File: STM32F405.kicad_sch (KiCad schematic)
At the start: 27 parts, among them SW1 SW_MEC_5G, SW2 SW_DIP_x04, U6 STM32F405RGTx, Y1 25MHz

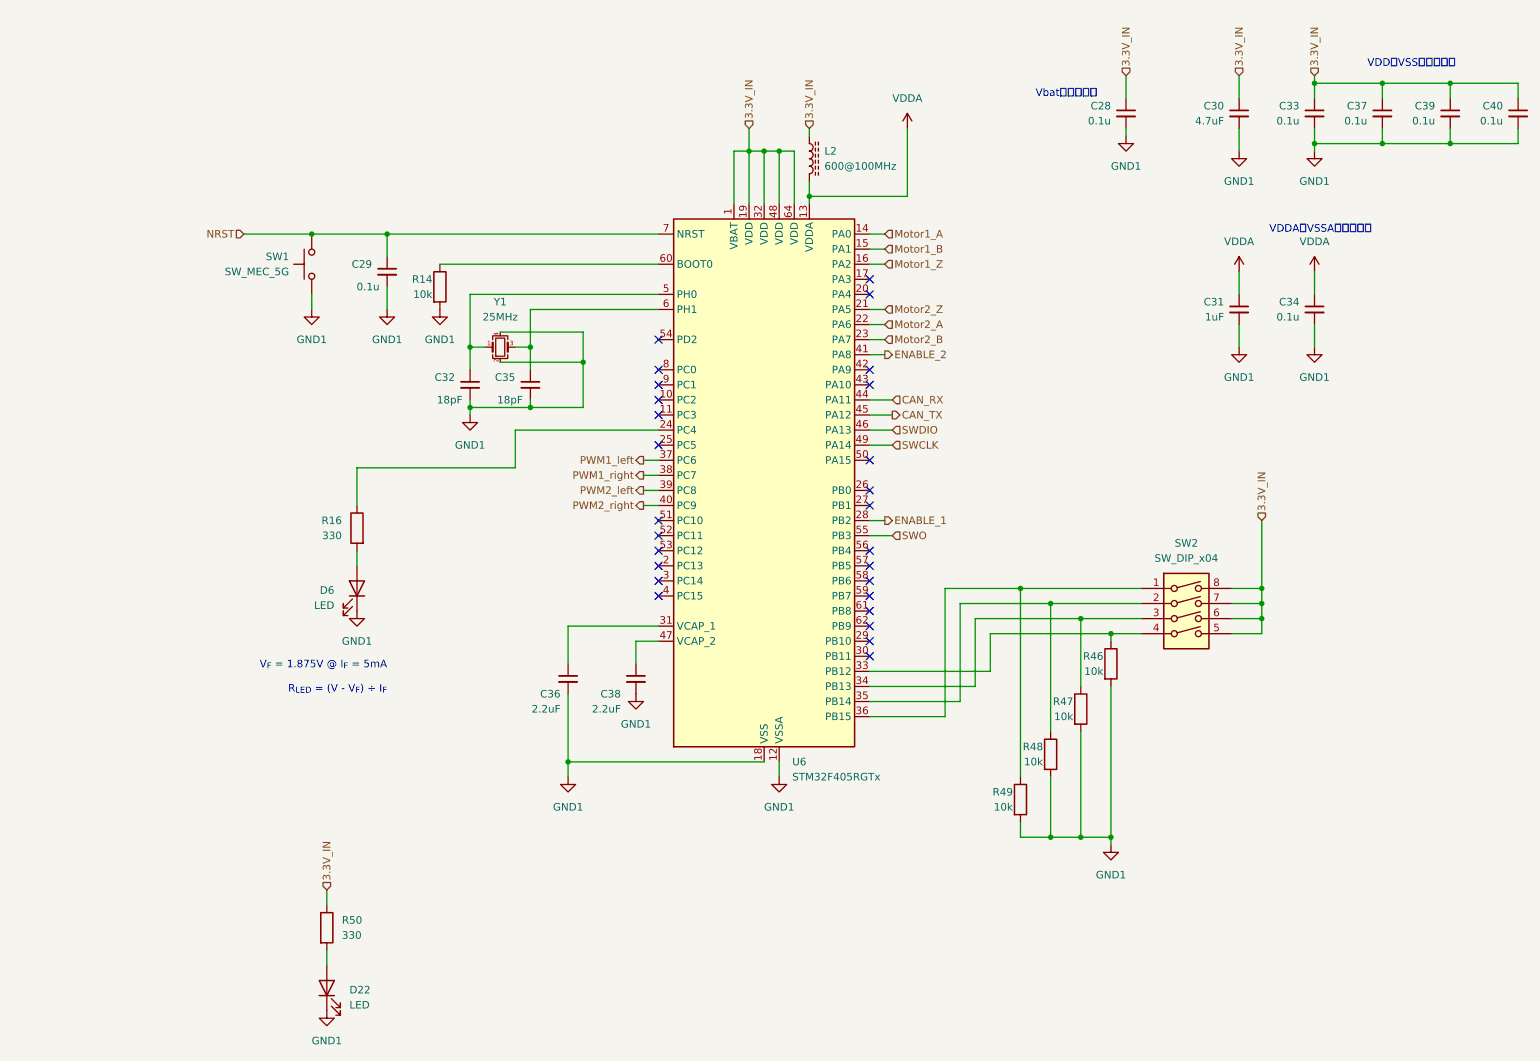
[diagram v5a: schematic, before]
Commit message: Update PCB design & add microSD connector
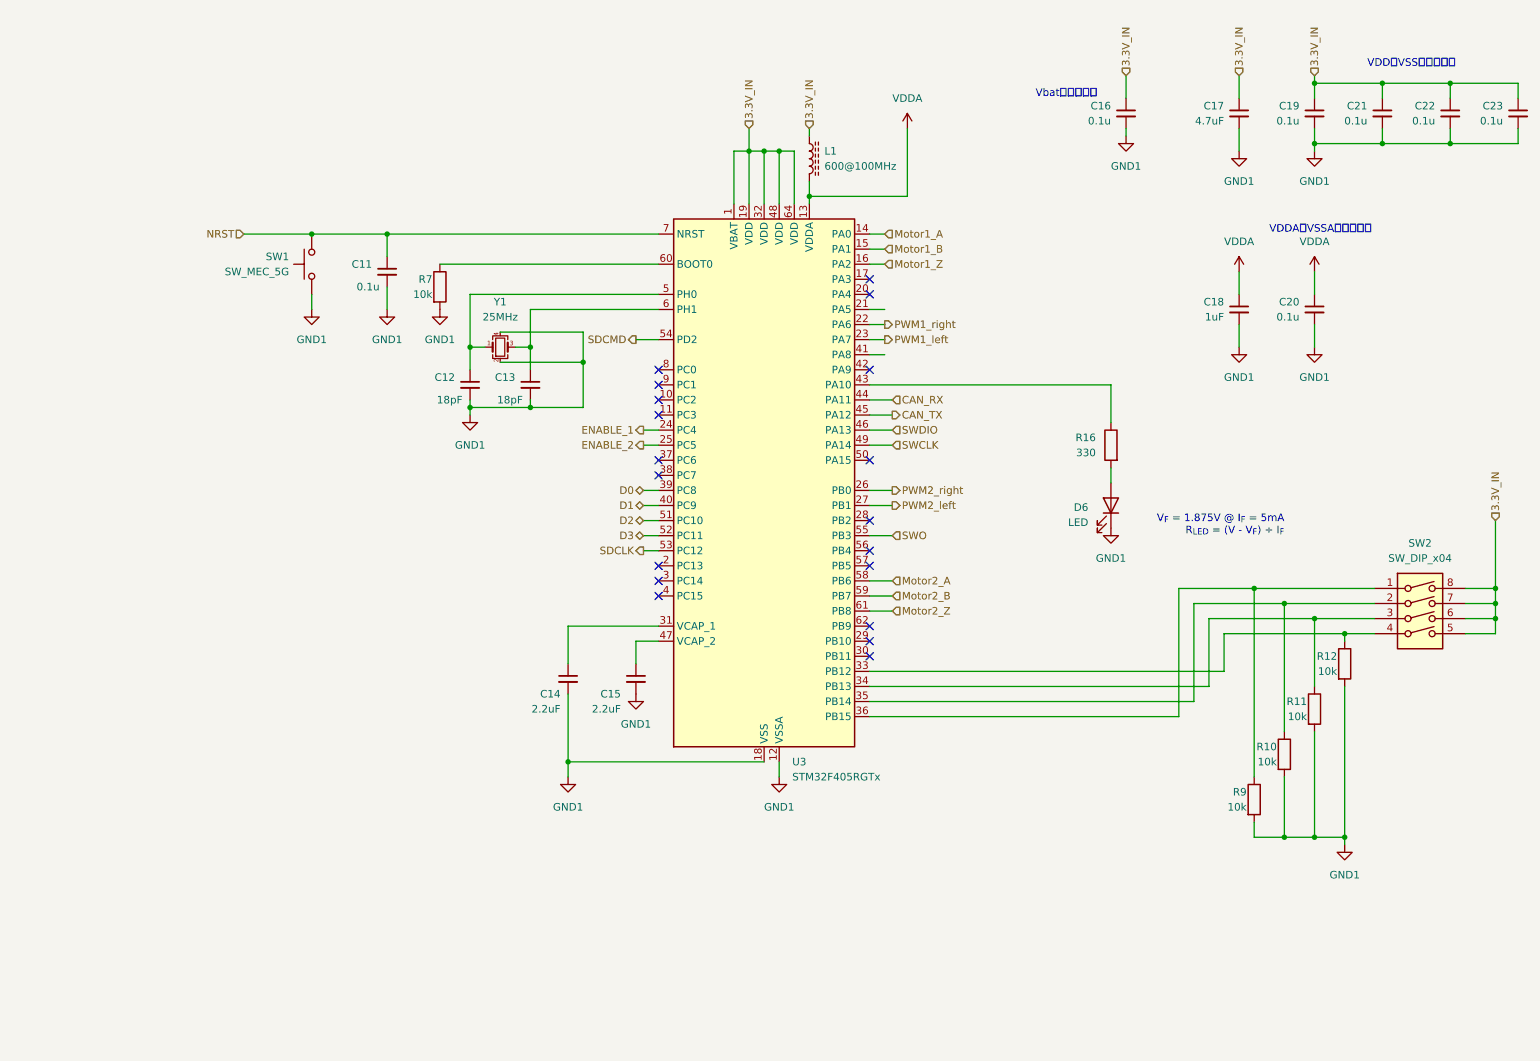
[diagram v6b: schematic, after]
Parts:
- removed D22: LED, LED_SMD:LED_0603_1608Metric_Pad1.05x0.95mm_HandSolder, symbol Device:LED
- removed R50: 330, Resistor_SMD:R_0603_1608Metric_Pad0.98x0.95mm_HandSolder, symbol Device:R
- C11: renamed from C29; footprint Capacitor_SMD:C_0402_1005Metric_Pad0.74x0.62mm_HandSolder -> Capacitor_SMD:C_0402_1005Metric
- C14: renamed from C36; footprint Capacitor_SMD:C_0603_1608Metric_Pad1.08x0.95mm_HandSolder -> Capacitor_SMD:C_0603_1608Metric
- C15: renamed from C38; footprint Capacitor_SMD:C_0603_1608Metric_Pad1.08x0.95mm_HandSolder -> Capacitor_SMD:C_0603_1608Metric
- C16: renamed from C28; footprint Capacitor_SMD:C_0402_1005Metric_Pad0.74x0.62mm_HandSolder -> Capacitor_SMD:C_0402_1005Metric
- C17: renamed from C30; footprint Capacitor_SMD:C_0603_1608Metric_Pad1.08x0.95mm_HandSolder -> Capacitor_SMD:C_0402_1005Metric
- C18: renamed from C31; footprint Capacitor_SMD:C_0603_1608Metric_Pad1.08x0.95mm_HandSolder -> Capacitor_SMD:C_0402_1005Metric
- C19: renamed from C33; footprint Capacitor_SMD:C_0402_1005Metric_Pad0.74x0.62mm_HandSolder -> Capacitor_SMD:C_0402_1005Metric
- C20: renamed from C34; footprint Capacitor_SMD:C_0402_1005Metric_Pad0.74x0.62mm_HandSolder -> Capacitor_SMD:C_0402_1005Metric
- C21: renamed from C37; footprint Capacitor_SMD:C_0402_1005Metric_Pad0.74x0.62mm_HandSolder -> Capacitor_SMD:C_0402_1005Metric
- C22: renamed from C39; footprint Capacitor_SMD:C_0402_1005Metric_Pad0.74x0.62mm_HandSolder -> Capacitor_SMD:C_0402_1005Metric
- C23: renamed from C40; footprint Capacitor_SMD:C_0402_1005Metric_Pad0.74x0.62mm_HandSolder -> Capacitor_SMD:C_0402_1005Metric
- L1: renamed from L2; footprint Resistor_SMD:R_0805_2012Metric_Pad1.20x1.40mm_HandSolder -> Resistor_SMD:R_0805_2012Metric
- R10: renamed from R48; footprint Resistor_SMD:R_0402_1005Metric_Pad0.72x0.64mm_HandSolder -> Resistor_SMD:R_0402_1005Metric
- R11: renamed from R47; footprint Resistor_SMD:R_0402_1005Metric_Pad0.72x0.64mm_HandSolder -> Resistor_SMD:R_0402_1005Metric
- R12: renamed from R46; footprint Resistor_SMD:R_0402_1005Metric_Pad0.72x0.64mm_HandSolder -> Resistor_SMD:R_0402_1005Metric
- R16: footprint Resistor_SMD:R_0603_1608Metric_Pad0.98x0.95mm_HandSolder -> Resistor_SMD:R_0603_1608Metric
- R7: renamed from R14; footprint Resistor_SMD:R_0402_1005Metric_Pad0.72x0.64mm_HandSolder -> Resistor_SMD:R_0402_1005Metric
- R9: renamed from R49; footprint Resistor_SMD:R_0402_1005Metric_Pad0.72x0.64mm_HandSolder -> Resistor_SMD:R_0402_1005Metric
- SW1: footprint Button_Switch_SMD:SW_Push_1P1T_XKB_TS-1187A -> RDC_footprint:TVBP06-B043
- renumbered C32 to C12, C35 to C13, U6 to U3
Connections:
- net ENABLE_1: now also U3.24 (PC4); no longer U3.28 (PB2)
- net ENABLE_2: now also U3.25 (PC5); no longer U3.41 (PA8)
- net Motor2_A: now also U3.58 (PB6); no longer U3.22 (PA6)
- net Motor2_B: now also U3.59 (PB7); no longer U3.23 (PA7)
- net Motor2_Z: now also U3.61 (PB8); no longer U3.21 (PA5)
- net PWM1_left: now also U3.23 (PA7); no longer U3.37 (PC6)
- net PWM1_right: now also U3.22 (PA6); no longer U3.38 (PC7)
- net PWM2_left: now also U3.27 (PB1); no longer U3.39 (PC8)
- net PWM2_right: now also U3.26 (PB0); no longer U3.40 (PC9)
- net at R16.1: now also U3.43 (PA10); no longer U3.24 (PC4)
- net D2: now reaches U3.51 (PC10)
- net D3: now reaches U3.52 (PC11)
- net SDCLK: now reaches U3.53 (PC12)
- net SDCMD: now reaches U3.54 (PD2)
- new net D0: U3.39 (PC8)
- new net D1: U3.40 (PC9)
- no-connect marks 27 -> 19
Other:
- moved on the sheet: D6, R10, R11, R12, R16, R9, SW2

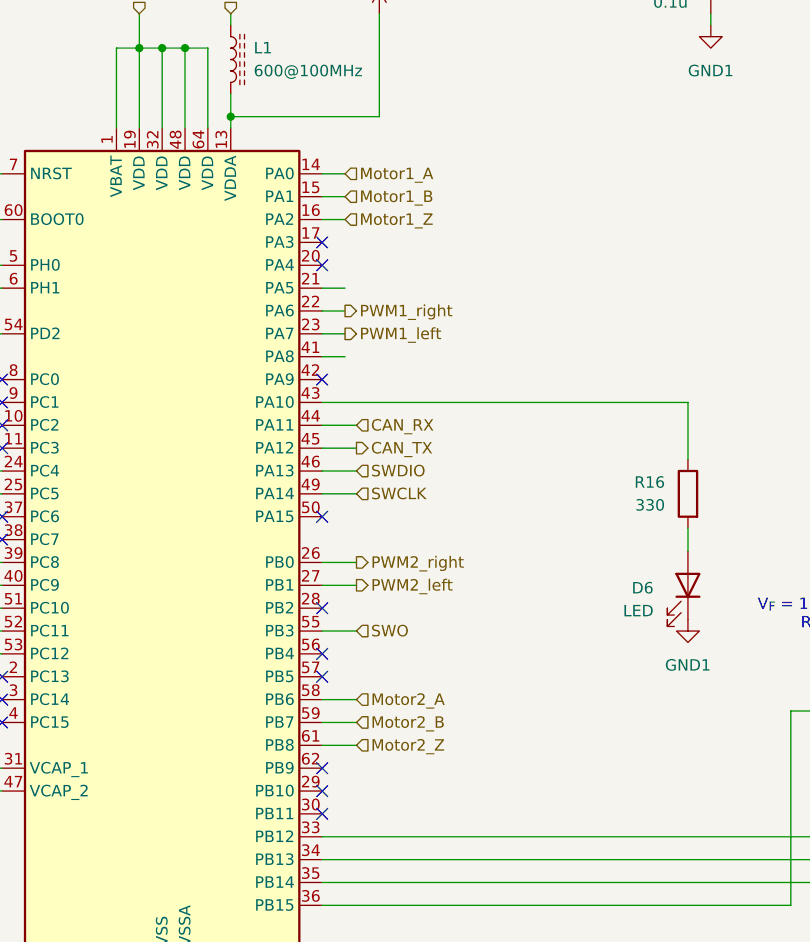
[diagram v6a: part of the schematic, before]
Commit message: add SEPIC IC symbol
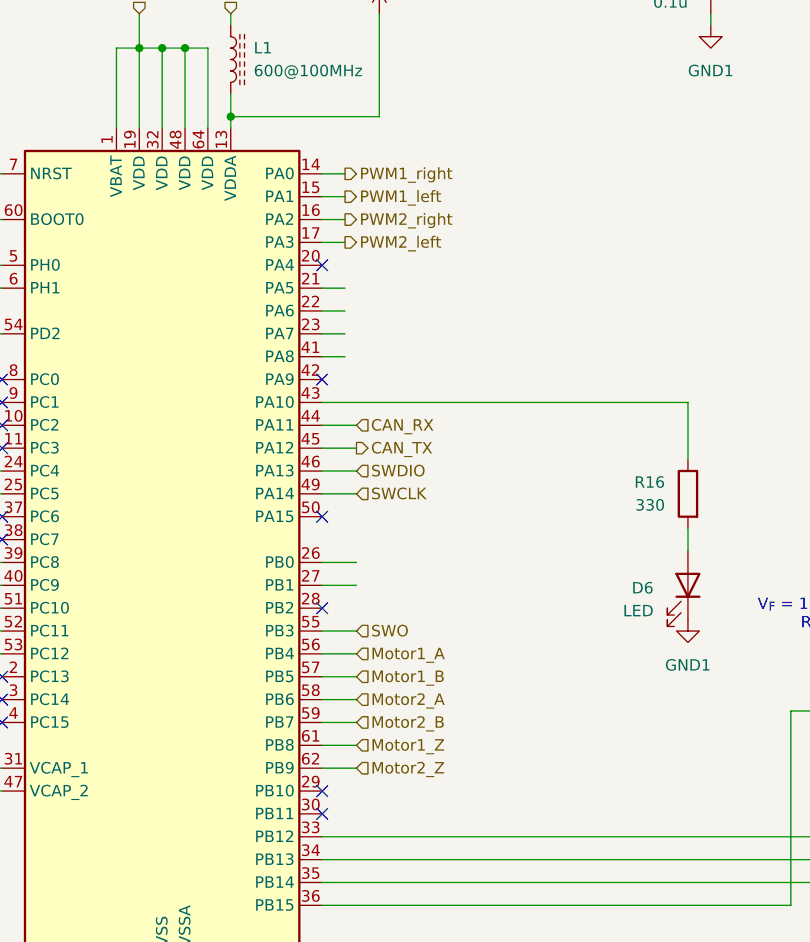
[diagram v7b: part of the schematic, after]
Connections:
- net Motor1_A: now also U3.56 (PB4); no longer U3.14 (PA0)
- net Motor1_B: now also U3.57 (PB5); no longer U3.15 (PA1)
- net Motor1_Z: now also U3.61 (PB8); no longer U3.16 (PA2)
- net Motor2_Z: now also U3.62 (PB9); no longer U3.61 (PB8)
- net PWM1_left: now also U3.15 (PA1); no longer U3.23 (PA7)
- net PWM1_right: now also U3.14 (PA0); no longer U3.22 (PA6)
- net PWM2_left: now also U3.17 (PA3); no longer U3.27 (PB1)
- net PWM2_right: now also U3.16 (PA2); no longer U3.26 (PB0)
- no-connect marks 19 -> 15
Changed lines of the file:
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@@
   (no_connect (at 168.91 125.73))
   (no_connect (at 168.91 123.19))
-  (no_connect (at 168.91 107.95))
   (no_connect (at 133.35 82.55))
-  (no_connect (at 168.91 110.49))
   (no_connect (at 133.35 95.25))
   (no_connect (at 133.35 77.47))
@@
   (no_connect (at 168.91 102.87))
   (no_connect (at 168.91 64.77))
-  (no_connect (at 168.91 120.65))
   (no_connect (at 133.35 85.09))
   (no_connect (at 133.35 115.57))
-  (no_connect (at 168.91 62.23))
   (no_connect (at 133.35 110.49))
   (no_connect (at 168.91 77.47))
@@
     (stroke (width 0) (type default))
   )
+  (wire (pts (xy 168.91 62.23) (xy 171.45 62.23))
+    (stroke (width 0) (type default))
+  )
   (wire (pts (xy 120.65 76.2) (xy 120.65 83.82))
     (stroke (width 0) (type default))
@@
     (stroke (width 0) (type default))
   )
+  (wire (pts (xy 168.91 120.65) (xy 172.72 120.65))
+    (stroke (width 0) (type default))
+  )
   (wire (pts (xy 148.59 36.83) (xy 148.59 40.64))
     (stroke (width 0) (type default))
@@
     (stroke (width 0) (type default))
   )
+  (wire (pts (xy 168.91 107.95) (xy 172.72 107.95))
+    (stroke (width 0) (type default))
+  )
   (wire (pts (xy 151.13 40.64) (xy 151.13 49.53))
     (stroke (width 0) (type default))
@@
     (stroke (width 0) (type default))
   )
+  (wire (pts (xy 168.91 118.11) (xy 172.72 118.11))
+    (stroke (width 0) (type default))
+  )
   (wire (pts (xy 101.6 73.66) (xy 101.6 77.47))
     (stroke (width 0) (type default))
   )
-  (wire (pts (xy 168.91 118.11) (xy 172.72 118.11))
-    (stroke (width 0) (type default))
-  )
   (wire (pts (xy 111.76 83.82) (xy 101.6 83.82))
     (stroke (width 0) (type default))
@@
   )
   (wire (pts (xy 130.81 102.87) (xy 133.35 102.87))
+    (stroke (width 0) (type default))
+  )
+  (wire (pts (xy 168.91 110.49) (xy 172.72 110.49))
     (stroke (width 0) (type default))
   )
@@
     (effects (font (size 1.27 1.27)) (justify left))
   )
+  (hierarchical_label "PWM1_right" (shape output) (at 171.45 54.61 0) (fields_autoplaced)
+    (effects (font (size 1.27 1.27)) (justify left))
+  )
   (hierarchical_label "SDCLK" (shape output) (at 130.81 107.95 180) (fields_autoplaced)
     (effects (font (size 1.27 1.27)) (justify right))
   )
+  (hierarchical_label "Motor1_A" (shape input) (at 172.72 107.95 0) (fields_autoplaced)
+    (effects (font (size 1.27 1.27)) (justify left))
+  )
+  (hierarchical_label "PWM2_left" (shape output) (at 171.45 62.23 0) (fields_autoplaced)
+    (effects (font (size 1.27 1.27)) (justify left))
+  )
   (hierarchical_label "3.3V_IN" (shape input) (at 148.59 36.83 90) (fields_autoplaced)
     (effects (font (size 1.27 1.27)) (justify left))
@@
     (effects (font (size 1.27 1.27)) (justify left))
   )
+  (hierarchical_label "PWM2_right" (shape output) (at 171.45 59.69 0) (fields_autoplaced)
+    (effects (font (size 1.27 1.27)) (justify left))
+  )
   (hierarchical_label "3.3V_IN" (shape input) (at 158.75 36.83 90) (fields_autoplaced)
     (effects (font (size 1.27 1.27)) (justify left))
   )
-  (hierarchical_label "Motor1_A" (shape input) (at 171.45 54.61 0) (fields_autoplaced)
-    (effects (font (size 1.27 1.27)) (justify left))
-  )
   (hierarchical_label "3.3V_IN" (shape input) (at 274.32 102.87 90) (fields_autoplaced)
     (effects (font (size 1.27 1.27)) (justify left))
@@
     (effects (font (size 1.27 1.27)) (justify left))
   )
+  (hierarchical_label "PWM1_left" (shape output) (at 171.45 57.15 0) (fields_autoplaced)
+    (effects (font (size 1.27 1.27)) (justify left))
+  )
   (hierarchical_label "3.3V_IN" (shape input) (at 212.09 27.94 90) (fields_autoplaced)
     (effects (font (size 1.27 1.27)) (justify left))
   )
-  (hierarchical_label "Motor1_Z" (shape input) (at 171.45 59.69 0) (fields_autoplaced)
+  (hierarchical_label "Motor1_B" (shape input) (at 172.72 110.49 0) (fields_autoplaced)
     (effects (font (size 1.27 1.27)) (justify left))
   )
@@
     (effects (font (size 1.27 1.27)) (justify left))
   )
-  (hierarchical_label "PWM1_left" (shape output) (at 171.45 72.39 0) (fields_autoplaced)
-    (effects (font (size 1.27 1.27)) (justify left))
-  )
   (hierarchical_label "SWCLK" (shape input) (at 172.72 90.17 0) (fields_autoplaced)
     (effects (font (size 1.27 1.27)) (justify left))
   )
-  (hierarchical_label "Motor1_B" (shape input) (at 171.45 57.15 0) (fields_autoplaced)
-    (effects (font (size 1.27 1.27)) (justify left))
-  )
-  (hierarchical_label "Motor2_Z" (shape input) (at 172.72 118.11 0) (fields_autoplaced)
-    (effects (font (size 1.27 1.27)) (justify left))
-  )
-  (hierarchical_label "PWM2_left" (shape output) (at 172.72 100.33 0) (fields_autoplaced)
-    (effects (font (size 1.27 1.27)) (justify left))
-  )
-  (hierarchical_label "PWM1_right" (shape output) (at 171.45 69.85 0) (fields_autoplaced)
+  (hierarchical_label "Motor2_Z" (shape input) (at 172.72 120.65 0) (fields_autoplaced)
     (effects (font (size 1.27 1.27)) (justify left))
   )
@@
     (effects (font (size 1.27 1.27)) (justify right))
   )
+  (hierarchical_label "Motor1_Z" (shape input) (at 172.72 118.11 0) (fields_autoplaced)
+    (effects (font (size 1.27 1.27)) (justify left))
+  )
   (hierarchical_label "ENABLE_2" (shape output) (at 130.81 90.17 180) (fields_autoplaced)
     (effects (font (size 1.27 1.27)) (justify right))
@@
     (effects (font (size 1.27 1.27)) (justify right))
   )
-  (hierarchical_label "PWM2_right" (shape output) (at 172.72 97.79 0) (fields_autoplaced)
-    (effects (font (size 1.27 1.27)) (justify left))
-  )
   (hierarchical_label "CAN_TX" (shape output) (at 172.72 85.09 0) (fields_autoplaced)

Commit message: 制御回路完成
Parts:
- removed R10, R11, R12, R9: 10k, Resistor_SMD:R_0402_1005Metric, symbol Device:R
- removed SW1: SW_MEC_5G, RDC_footprint:TVBP06-B043, symbol Switch:SW_MEC_5G
- removed SW2: SW_DIP_x04, Button_Switch_SMD:SW_DIP_SPSTx04_Slide_Copal_CHS-04B_W7.62mm_P1.27mm, symbol Switch:SW_DIP_x04
- added R67: 10k, Resistor_SMD:R_0402_1005Metric, symbol Device:R
- added SW1, SW3: SW_Push, RDC_footprint:TVBP06-B043, symbol Switch:SW_Push
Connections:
- net 3.3V_IN: now also SW3.2
- net GND1: now also R67.2, SW1.1
- net NRST: now also SW1.2
- net at R16.1: now also U3.33 (PB12); no longer U3.43 (PA10)
- net CAN_ID2: now reaches U3.10 (PC2)
- net CAN_ID1: now reaches U3.11 (PC3)
- net SD_Detector: now reaches U3.20 (PA4)
- net at U3.21 (PA5): now also R67.1, SW3.1
- net CAN_ID4: now reaches U3.8 (PC0)
- net CAN_ID3: now reaches U3.9 (PC1)
- no-connect marks 15 -> 19
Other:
- moved on the sheet: C11, C12, C13, C14, C15, L1, R7, U3, Y1
